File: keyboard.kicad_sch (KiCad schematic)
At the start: 207 parts, among them J2 USB_C_Receptacle_USB2.0_16P, J4 Conn_01x05, SW1 SW_Push, SW2 SW_Push, U1 RP2040, U2 XC6206PxxxMR, U3 W25Q128JVS, Y1 Crystal_GND24

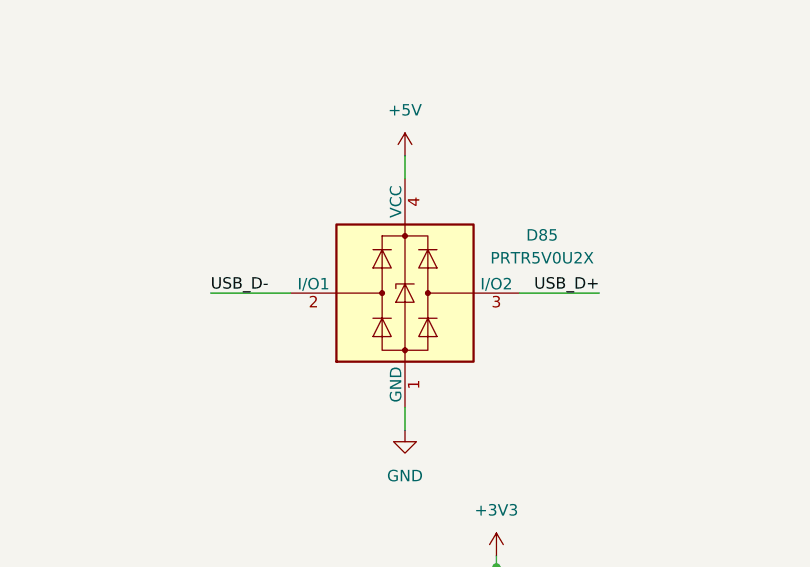
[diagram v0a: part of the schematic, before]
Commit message: add traces to usb subcircuit and subtraces
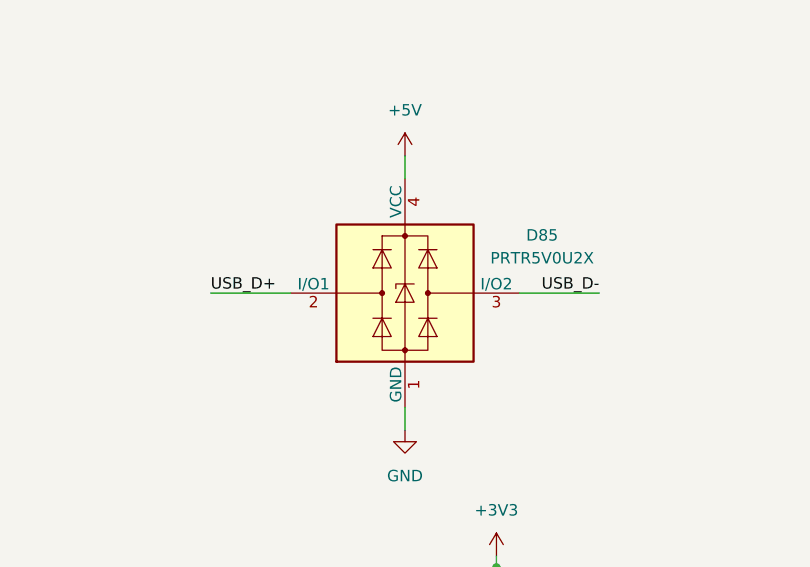
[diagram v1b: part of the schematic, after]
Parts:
- R1, R10, R11, R2, R6, R8, R9: footprint Resistor_SMD:R_0402_1005Metric -> Resistor_SMD:R_0402_1005Metric_Pad0.72x0.64mm_HandSolder
- R3, R7: footprint Resistor_SMD:R_0402_1005Metric -> Resistor_SMD:R_0805_2012Metric_Pad1.20x1.40mm_HandSolder
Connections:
- net USB_D+: now also D85.2 (I/O1); no longer D85.3 (I/O2)
- net USB_D-: now also D85.3 (I/O2); no longer D85.2 (I/O1)
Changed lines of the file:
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@@
 	)
 	(label "USB_D+"
-		(at 149.86 248.92 180)
+		(at 106.68 248.92 0)
 		(effects
 			(font
 				(size 1.27 1.27)
 			)
-			(justify right bottom)
+			(justify left bottom)
 		)
 	)
@@
 	)
 	(label "USB_D-"
-		(at 106.68 248.92 0)
+		(at 149.86 248.92 180)
 		(effects
 			(font
 				(size 1.27 1.27)
 			)
-			(justify left bottom)
+			(justify right bottom)
 		)
 	)
@@
 			)
 		)
-		(property "Footprint" "Resistor_SMD:R_0402_1005Metric"
+		(property "Footprint" "Resistor_SMD:R_0805_2012Metric_Pad1.20x1.40mm_HandSolder"
 			(at 88.9 187.96 0)
 			(hide yes)
@@
 			)
 		)
-		(property "Footprint" "Resistor_SMD:R_0402_1005Metric"
+		(property "Footprint" "Resistor_SMD:R_0402_1005Metric_Pad0.72x0.64mm_HandSolder"
 			(at 212.09 63.5 0)
 			(hide yes)
@@
 			)
 		)
-		(property "Footprint" "Resistor_SMD:R_0402_1005Metric"
+		(property "Footprint" "Resistor_SMD:R_0402_1005Metric_Pad0.72x0.64mm_HandSolder"
 			(at 299.72 60.96 0)
 			(hide yes)
@@
 			)
 		)
-		(property "Footprint" "Resistor_SMD:R_0402_1005Metric"
+		(property "Footprint" "Resistor_SMD:R_0402_1005Metric_Pad0.72x0.64mm_HandSolder"
 			(at 299.72 53.34 0)
 			(hide yes)
@@
 			)
 		)
-		(property "Footprint" "Resistor_SMD:R_0402_1005Metric"
+		(property "Footprint" "Resistor_SMD:R_0402_1005Metric_Pad0.72x0.64mm_HandSolder"
 			(at 82.55 91.948 90)
 			(hide yes)
@@
 			)
 		)
-		(property "Footprint" "Resistor_SMD:R_0402_1005Metric"
+		(property "Footprint" "Resistor_SMD:R_0402_1005Metric_Pad0.72x0.64mm_HandSolder"
 			(at 294.64 67.31 0)
 			(hide yes)
@@
 			)
 		)
-		(property "Footprint" "Resistor_SMD:R_0402_1005Metric"
+		(property "Footprint" "Resistor_SMD:R_0402_1005Metric_Pad0.72x0.64mm_HandSolder"
 			(at 82.55 83.058 90)
 			(hide yes)
@@
 			)
 		)
-		(property "Footprint" "Resistor_SMD:R_0402_1005Metric"
+		(property "Footprint" "Resistor_SMD:R_0402_1005Metric_Pad0.72x0.64mm_HandSolder"
 			(at 87.63 318.008 90)
 			(hide yes)
@@
 			)
 		)
-		(property "Footprint" "Resistor_SMD:R_0402_1005Metric"
+		(property "Footprint" "Resistor_SMD:R_0805_2012Metric_Pad1.20x1.40mm_HandSolder"
 			(at 96.52 185.42 0)
 			(hide yes)

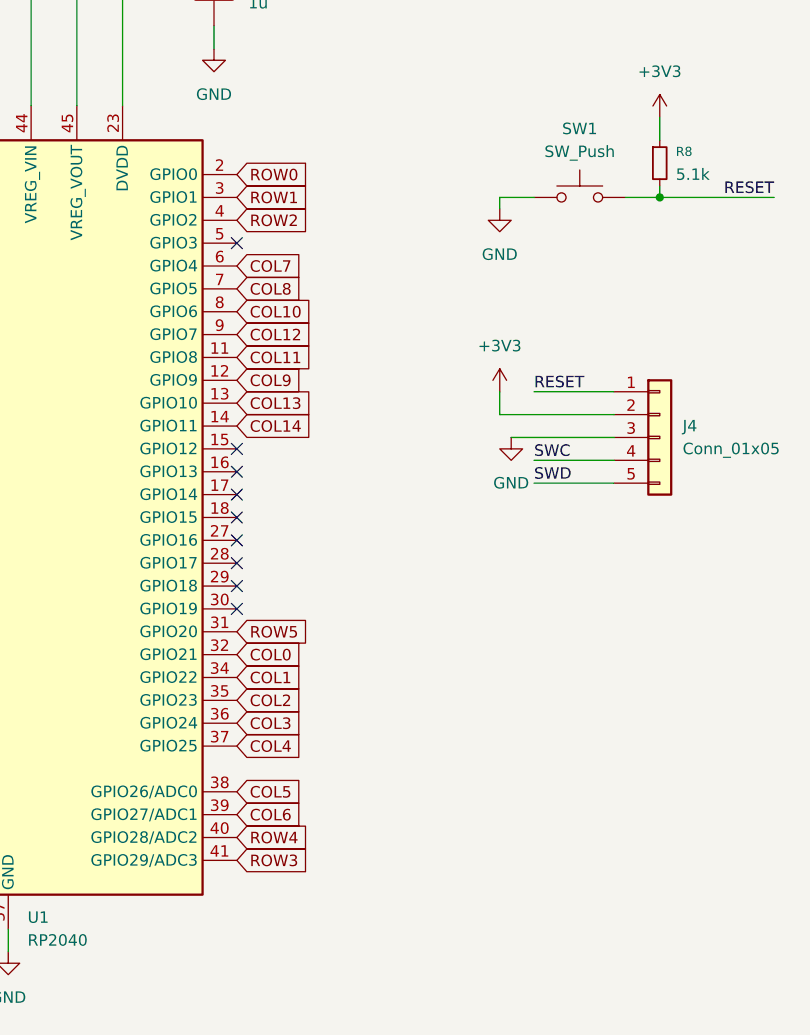
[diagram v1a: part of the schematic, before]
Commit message: routing complete, need to run DRC
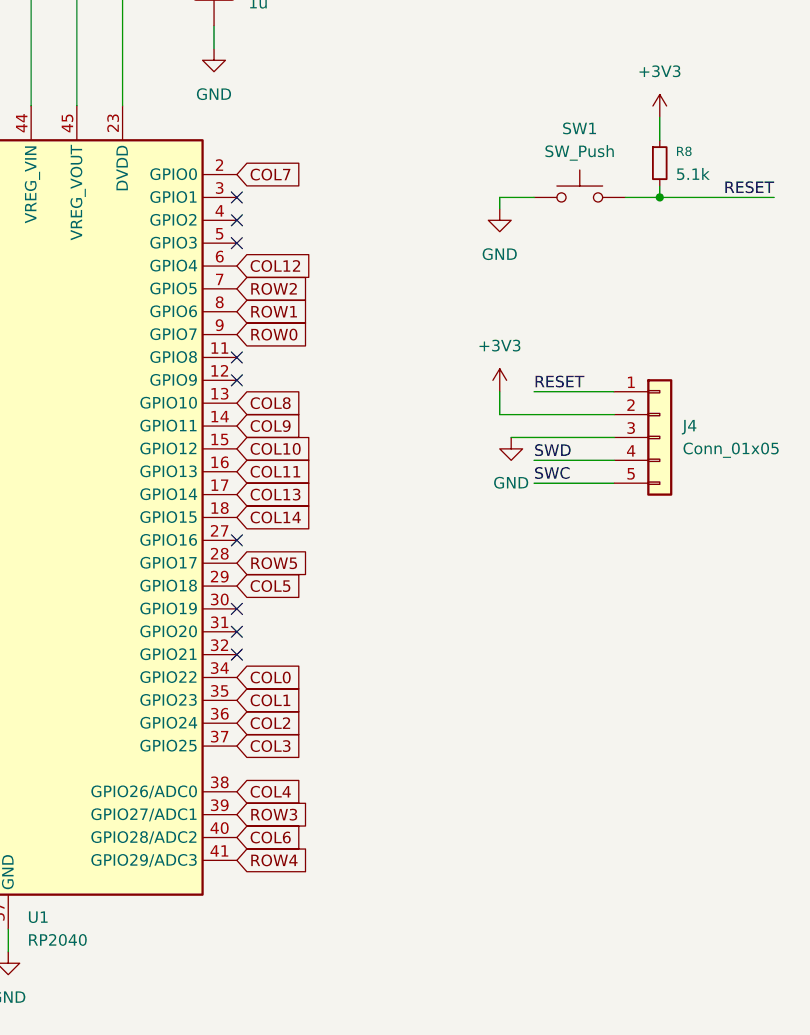
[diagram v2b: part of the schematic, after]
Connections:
- net COL0: now also U1.34 (GPIO22); no longer U1.32 (GPIO21)
- net COL1: now also U1.35 (GPIO23); no longer U1.34 (GPIO22)
- net COL10: now also U1.15 (GPIO12); no longer U1.8 (GPIO6)
- net COL11: now also U1.16 (GPIO13); no longer U1.11 (GPIO8)
- net COL12: now also U1.6 (GPIO4); no longer U1.9 (GPIO7)
- net COL13: now also U1.17 (GPIO14); no longer U1.13 (GPIO10)
- net COL14: now also U1.18 (GPIO15); no longer U1.14 (GPIO11)
- net COL2: now also U1.36 (GPIO24); no longer U1.35 (GPIO23)
- net COL3: now also U1.37 (GPIO25); no longer U1.36 (GPIO24)
- net COL4: now also U1.38 (GPIO26/ADC0); no longer U1.37 (GPIO25)
- net COL5: now also U1.29 (GPIO18); no longer U1.38 (GPIO26/ADC0)
- net COL6: now also U1.40 (GPIO28/ADC2); no longer U1.39 (GPIO27/ADC1)
- net COL7: now also U1.2 (GPIO0); no longer U1.6 (GPIO4)
- net COL8: now also U1.13 (GPIO10); no longer U1.7 (GPIO5)
- net COL9: now also U1.14 (GPIO11); no longer U1.12 (GPIO9)
- net ROW0: now also U1.9 (GPIO7); no longer U1.2 (GPIO0)
- net ROW1: now also U1.8 (GPIO6); no longer U1.3 (GPIO1)
- net ROW2: now also U1.7 (GPIO5); no longer U1.4 (GPIO2)
- net ROW3: now also U1.39 (GPIO27/ADC1); no longer U1.41 (GPIO29/ADC3)
- net ROW4: now also U1.41 (GPIO29/ADC3); no longer U1.40 (GPIO28/ADC2)
- net ROW5: now also U1.28 (GPIO17); no longer U1.31 (GPIO20)
- net SWC: now also J4.5 (Pin_5); no longer J4.4 (Pin_4)
- net SWD: now also J4.4 (Pin_4); no longer J4.5 (Pin_5)
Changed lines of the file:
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@@
 	)
 	(junction
-		(at 321.31 165.1)
-		(diameter 0)
-		(color 0 0 0 0)
-	)
-	(junction
 		(at 46.99 213.36)
 		(diameter 0)
@@
 	)
 	(junction
+		(at 321.31 165.1)
+		(diameter 0)
+		(color 0 0 0 0)
+	)
+	(junction
 		(at 304.8 184.15)
 		(diameter 0)
@@
 	)
 	(junction
-		(at 304.8 165.1)
-		(diameter 0)
-		(color 0 0 0 0)
-	)
-	(junction
 		(at 354.33 165.1)
 		(diameter 0)
@@
 	)
 	(junction
+		(at 304.8 165.1)
+		(diameter 0)
+		(color 0 0 0 0)
+	)
+	(junction
 		(at 105.41 173.99)
 		(diameter 0)
@@
 	)
 	(no_connect
-		(at 165.1 100.33)
+		(at 165.1 67.31)
 	)
 	(no_connect
-		(at 165.1 95.25)
+		(at 165.1 69.85)
 	)
 	(no_connect
-		(at 165.1 107.95)
+		(at 165.1 118.11)
 	)
 	(no_connect
-		(at 165.1 102.87)
+		(at 165.1 85.09)
 	)
 	(no_connect
-		(at 165.1 110.49)
+		(at 165.1 115.57)
 	)
 	(no_connect
-		(at 165.1 97.79)
+		(at 165.1 87.63)
 	)
 	(no_connect
@@
 	(wire
 		(pts
+			(xy 304.8 165.1) (xy 321.31 165.1)
+		)
+		(stroke
+			(width 0)
+			(type default)
+		)
+	)
+	(wire
+		(pts
 			(xy 469.9 203.2) (xy 518.16 203.2)
 		)
@@
 	(wire
 		(pts
-			(xy 304.8 165.1) (xy 321.31 165.1)
-		)
-		(stroke
-			(width 0)
-			(type default)
-		)
-	)
-	(wire
-		(pts
 			(xy 415.29 123.19) (xy 415.29 134.62)
 		)
@@
 	)
 	(label "SWD"
-		(at 198.12 99.06 0)
+		(at 198.12 96.52 0)
 		(effects
 			(font
@@
 	)
 	(label "SWC"
-		(at 198.12 96.52 0)
+		(at 198.12 99.06 0)
 		(effects
 			(font
@@
 	(global_label "COL2"
 		(shape input)
-		(at 165.1 123.19 0)
+		(at 165.1 125.73 0)
 		(fields_autoplaced yes)
 		(effects
@@
 		)
 		(property "Intersheetrefs" "${INTERSHEET_REFS}"
-			(at 172.9233 123.19 0)
+			(at 172.9233 125.73 0)
 			(hide yes)
 			(show_name no)
@@
 	(global_label "ROW5"
 		(shape input)
-		(at 165.1 115.57 0)
+		(at 165.1 107.95 0)
 		(fields_autoplaced yes)
 		(effects
@@
 		)
 		(property "Intersheetrefs" "${INTERSHEET_REFS}"
-			(at 172.9233 115.57 0)
+			(at 172.9233 107.95 0)
 			(hide yes)
 			(show_name no)
@@
 	(global_label "COL0"
 		(shape input)
-		(at 165.1 118.11 0)
+		(at 165.1 120.65 0)
 		(fields_autoplaced yes)
 		(effects
@@
 		)
 		(property "Intersheetrefs" "${INTERSHEET_REFS}"
-			(at 173.3466 118.11 0)
+			(at 173.3466 120.65 0)
 			(hide yes)
 			(show_name no)
@@
 	(global_label "COL12"
 		(shape input)
-		(at 165.1 82.55 0)
+		(at 165.1 74.93 0)
 		(fields_autoplaced yes)
 		(effects
@@
 		)
 		(property "Intersheetrefs" "${INTERSHEET_REFS}"
-			(at 172.9233 82.55 0)
+			(at 174.1328 74.93 0)
 			(hide yes)
 			(show_name no)
@@
 	(global_label "ROW1"
 		(shape input)
-		(at 165.1 67.31 0)
+		(at 165.1 80.01 0)
 		(fields_autoplaced yes)
 		(effects
@@
 		)
 		(property "Intersheetrefs" "${INTERSHEET_REFS}"
-			(at 173.3466 67.31 0)
+			(at 173.3466 80.01 0)
 			(hide yes)
 			(show_name no)
@@
 	(global_label "COL4"
 		(shape input)
-		(at 165.1 128.27 0)
+		(at 165.1 133.35 0)
 		(fields_autoplaced yes)
 		(effects
@@
 		)
 		(property "Intersheetrefs" "${INTERSHEET_REFS}"
-			(at 172.9233 128.27 0)
+			(at 172.9233 133.35 0)
 			(hide yes)
 			(show_name no)
@@
 	(global_label "ROW3"
 		(shape input)
-		(at 165.1 140.97 0)
+		(at 165.1 135.89 0)
 		(fields_autoplaced yes)
 		(effects
@@
 		)
 		(property "Intersheetrefs" "${INTERSHEET_REFS}"
-			(at 173.3466 140.97 0)
+			(at 172.9233 135.89 0)
 			(hide yes)
 			(show_name no)
@@
 	(global_label "COL11"
 		(shape input)
-		(at 165.1 85.09 0)
+		(at 165.1 97.79 0)
 		(fields_autoplaced yes)
 		(effects
@@
 		)
 		(property "Intersheetrefs" "${INTERSHEET_REFS}"
-			(at 172.9233 85.09 0)
+			(at 172.9233 97.79 0)
 			(hide yes)
 			(show_name no)
@@
 	(global_label "COL10"
 		(shape input)
-		(at 165.1 80.01 0)
+		(at 165.1 95.25 0)
 		(fields_autoplaced yes)
 		(effects
@@
 		)
 		(property "Intersheetrefs" "${INTERSHEET_REFS}"
-			(at 174.1328 80.01 0)
+			(at 172.9233 95.25 0)
 			(hide yes)
 			(show_name no)
@@
 	(global_label "ROW0"
 		(shape input)
-		(at 165.1 64.77 0)
+		(at 165.1 82.55 0)
 		(fields_autoplaced yes)
 		(effects
@@
 		)
 		(property "Intersheetrefs" "${INTERSHEET_REFS}"
-			(at 173.3466 64.77 0)
+			(at 174.1328 82.55 0)
 			(hide yes)
 			(show_name no)
@@
 	(global_label "COL5"
 		(shape input)
-		(at 165.1 133.35 0)
+		(at 165.1 110.49 0)
 		(fields_autoplaced yes)
 		(effects
@@
 		)
 		(property "Intersheetrefs" "${INTERSHEET_REFS}"
-			(at 172.9233 133.35 0)
+			(at 173.3466 110.49 0)
 			(hide yes)
 			(show_name no)
@@
 	(global_label "ROW4"
 		(shape input)
-		(at 165.1 138.43 0)
+		(at 165.1 140.97 0)
 		(fields_autoplaced yes)
 		(effects
@@
 		)
 		(property "Intersheetrefs" "${INTERSHEET_REFS}"
-			(at 172.9233 138.43 0)
+			(at 173.3466 140.97 0)
 			(hide yes)
 			(show_name no)
@@
 	(global_label "COL3"
 		(shape input)
-		(at 165.1 125.73 0)
+		(at 165.1 128.27 0)
 		(fields_autoplaced yes)
 		(effects
@@
 		)
 		(property "Intersheetrefs" "${INTERSHEET_REFS}"
-			(at 172.9233 125.73 0)
+			(at 172.9233 128.27 0)
 			(hide yes)
 			(show_name no)
@@
 	(global_label "COL14"
 		(shape input)
-		(at 165.1 92.71 0)
+		(at 165.1 102.87 0)
 		(fields_autoplaced yes)
 		(effects
@@
 		)
 		(property "Intersheetrefs" "${INTERSHEET_REFS}"
-			(at 174.1328 92.71 0)
+			(at 174.1328 102.87 0)
 			(hide yes)
 			(show_name no)
@@
 	(global_label "COL7"
 		(shape input)
-		(at 165.1 74.93 0)
+		(at 165.1 64.77 0)
 		(fields_autoplaced yes)
 		(effects
@@
 		)
 		(property "Intersheetrefs" "${INTERSHEET_REFS}"
-			(at 174.1328 74.93 0)
+			(at 173.3466 64.77 0)
 			(hide yes)
 			(show_name no)
@@
 	(global_label "ROW2"
 		(shape input)
-		(at 165.1 69.85 0)
+		(at 165.1 77.47 0)
 		(fields_autoplaced yes)
 		(effects
@@
 		)
 		(property "Intersheetrefs" "${INTERSHEET_REFS}"
-			(at 173.3466 69.85 0)
+			(at 173.3466 77.47 0)
 			(hide yes)
 			(show_name no)
@@
 	(global_label "COL8"
 		(shape input)
-		(at 165.1 77.47 0)
+		(at 165.1 90.17 0)
 		(fields_autoplaced yes)
 		(effects
@@
 		)
 		(property "Intersheetrefs" "${INTERSHEET_REFS}"
-			(at 174.1328 77.47 0)
+			(at 172.9233 90.17 0)
 			(hide yes)
 			(show_name no)
@@
 	(global_label "COL1"
 		(shape input)
-		(at 165.1 120.65 0)
+		(at 165.1 123.19 0)
 		(fields_autoplaced yes)
 		(effects
@@
 		)
 		(property "Intersheetrefs" "${INTERSHEET_REFS}"
-			(at 173.3466 120.65 0)
+			(at 172.9233 123.19 0)
 			(hide yes)
 			(show_name no)
@@
 	(global_label "COL6"
 		(shape input)
-		(at 165.1 135.89 0)
+		(at 165.1 138.43 0)
 		(fields_autoplaced yes)
 		(effects
@@
 		)
 		(property "Intersheetrefs" "${INTERSHEET_REFS}"
-			(at 172.9233 135.89 0)
+			(at 172.9233 138.43 0)
 			(hide yes)
 			(show_name no)
@@
 	(global_label "COL13"
 		(shape input)
-		(at 165.1 90.17 0)
+		(at 165.1 100.33 0)
 		(fields_autoplaced yes)
 		(effects
@@
 		)
 		(property "Intersheetrefs" "${INTERSHEET_REFS}"
-			(at 174.1328 90.17 0)
+			(at 174.1328 100.33 0)
 			(hide yes)
 			(show_name no)
@@
 	(global_label "COL9"
 		(shape input)
-		(at 165.1 87.63 0)
+		(at 165.1 92.71 0)
 		(fields_autoplaced yes)
 		(effects
@@
 		)
 		(property "Intersheetrefs" "${INTERSHEET_REFS}"
-			(at 172.9233 87.63 0)
+			(at 174.1328 92.71 0)
 			(hide yes)
 			(show_name no)

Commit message: clean up schematic
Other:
- note added: "Crystal Oscillator"
- note added: "Debug Header"
- note added: "ESD Protection"
- note added: "Flash Chip"
- note added: "Keyboard Matrix"
- note added: "RP2040"
- note added: "USB-C Port"
- moved on the sheet: C1, C10, C11, C12, C13, C14, C15, C16, C2, C3, C4, C5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

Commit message: swap to hotswappable sockets, may not adjust components
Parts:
- MX1, MX10, MX11, MX12, MX13, MX14, MX15, MX16, MX17, MX18, MX19, MX2, MX20, MX21, MX22, MX23, MX24, MX25, MX26, MX27, MX28, MX29, MX3, MX30, MX31, MX33, MX34, MX35, MX36, MX37, MX38, MX39, MX4, MX40, MX41, MX42, MX43, MX44, MX46, MX48, MX49, MX5, MX50, MX51, MX52, MX53, MX54, MX55, MX56, MX57, MX58, MX59, MX6, MX60, MX61, MX62, MX63, MX64, MX65, MX66, MX67, MX68, MX69, MX7, MX70, MX71, MX73, MX74, MX78, MX79, MX8, MX80, MX81, MX82, MX83, MX84, MX9: footprint PCM_marbastlib-mx:SW_MX_1u -> PCM_marbastlib-mx:SW_MX_HS_CPG151101S11_1u
- MX32, MX45: footprint PCM_marbastlib-mx:SW_MX_1.5u -> PCM_marbastlib-mx:SW_MX_HS_CPG151101S11_1.5u
- MX47, MX72: footprint PCM_marbastlib-mx:SW_MX_1.75u -> PCM_marbastlib-mx:SW_MX_HS_CPG151101S11_1.75u
- MX75, MX76, MX77: footprint PCM_marbastlib-mx:SW_MX_1.25u -> PCM_marbastlib-mx:SW_MX_HS_CPG151101S11_1.25u

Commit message: add separate LED daisy link sch
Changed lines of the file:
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@@
 	(wire
 		(pts
-			(xy 33.02 393.7) (xy 33.02 394.97)
+			(xy 91.44 287.02) (xy 91.44 288.29)
 		)
 		(stroke
@@
 	(wire
 		(pts
-			(xy 46.99 393.7) (xy 46.99 394.97)
+			(xy 105.41 287.02) (xy 105.41 288.29)
 		)
 		(stroke
@@
 	(wire
 		(pts
-			(xy 59.69 393.7) (xy 59.69 394.97)
+			(xy 118.11 287.02) (xy 118.11 288.29)
 		)
 		(stroke
@@
 	(symbol
 		(lib_id "power:PWR_FLAG")
-		(at 59.69 393.7 0)
+		(at 118.11 287.02 0)
 		(unit 1)
 		(body_style 1)
@@
 		(fields_autoplaced yes)
 		(property "Reference" "#FLG03"
-			(at 59.69 391.795 0)
+			(at 118.11 285.115 0)
 			(hide yes)
 			(show_name no)
@@
 		)
 		(property "Value" "PWR_FLAG"
-			(at 59.69 388.62 0)
+			(at 118.11 281.94 0)
 			(show_name no)
 			(do_not_autoplace no)
@@
 		)
 		(property "Footprint" ""
-			(at 59.69 393.7 0)
+			(at 118.11 287.02 0)
 			(hide yes)
 			(show_name no)
@@
 		)
 		(property "Datasheet" ""
-			(at 59.69 393.7 0)
+			(at 118.11 287.02 0)
 			(hide yes)
 			(show_name no)
@@
 		)
 		(property "Description" "Special symbol for telling ERC where power comes from"
-			(at 59.69 393.7 0)
+			(at 118.11 287.02 0)
 			(hide yes)
 			(show_name no)
@@
 	(symbol
 		(lib_id "power:PWR_FLAG")
-		(at 33.02 393.7 0)
+		(at 91.44 287.02 0)
 		(unit 1)
 		(body_style 1)
@@
 		(fields_autoplaced yes)
 		(property "Reference" "#FLG01"
-			(at 33.02 391.795 0)
+			(at 91.44 285.115 0)
 			(hide yes)
 			(show_name no)
@@
 		)
 		(property "Value" "PWR_FLAG"
-			(at 33.02 388.62 0)
+			(at 91.44 281.94 0)
 			(show_name no)
 			(do_not_autoplace no)
@@
 		)
 		(property "Footprint" ""
-			(at 33.02 393.7 0)
+			(at 91.44 287.02 0)
 			(hide yes)
 			(show_name no)
@@
 		)
 		(property "Datasheet" ""
-			(at 33.02 393.7 0)
+			(at 91.44 287.02 0)
 			(hide yes)
 			(show_name no)
@@
 		)
 		(property "Description" "Special symbol for telling ERC where power comes from"
-			(at 33.02 393.7 0)
+			(at 91.44 287.02 0)
 			(hide yes)
 			(show_name no)
@@
 	(symbol
 		(lib_id "power:PWR_FLAG")
-		(at 46.99 393.7 0)
+		(at 105.41 287.02 0)
 		(unit 1)
 		(body_style 1)
@@
 		(fields_autoplaced yes)
 		(property "Reference" "#FLG02"
-			(at 46.99 391.795 0)
+			(at 105.41 285.115 0)
 			(hide yes)
 			(show_name no)
@@
 		)
 		(property "Value" "PWR_FLAG"
-			(at 46.99 388.62 0)
+			(at 105.41 281.94 0)
 			(show_name no)
 			(do_not_autoplace no)
@@
 		)
 		(property "Footprint" ""
-			(at 46.99 393.7 0)
+			(at 105.41 287.02 0)
 			(hide yes)
 			(show_name no)
@@
 		)
 		(property "Datasheet" ""
-			(at 46.99 393.7 0)
+			(at 105.41 287.02 0)
 			(hide yes)
 			(show_name no)
@@
 		)
 		(property "Description" "Special symbol for telling ERC where power comes from"
-			(at 46.99 393.7 0)
+			(at 105.41 287.02 0)
 			(hide yes)
 			(show_name no)
@@
 	(symbol
 		(lib_id "power:VBUS")
-		(at 46.99 394.97 180)
+		(at 105.41 288.29 180)
 		(unit 1)
 		(body_style 1)
@@
 		(fields_autoplaced yes)
 		(property "Reference" "#PWR033"
-			(at 46.99 391.16 0)
+			(at 105.41 284.48 0)
 			(hide yes)
 			(show_name no)
@@
 		)
 		(property "Value" "VBUS"
-			(at 46.99 400.05 0)
+			(at 105.41 293.37 0)
 			(show_name no)
 			(do_not_autoplace no)
@@
 		)
 		(property "Footprint" ""
-			(at 46.99 394.97 0)
+			(at 105.41 288.29 0)
 			(hide yes)
 			(show_name no)
@@
 		)
 		(property "Datasheet" ""
-			(at 46.99 394.97 0)
+			(at 105.41 288.29 0)
 			(hide yes)
 			(show_name no)
@@
 		)
 		(property "Description" "Power symbol creates a global label with name \"VBUS\""
-			(at 46.99 394.97 0)
+			(at 105.41 288.29 0)
 			(hide yes)
 			(show_name no)
@@
 	(symbol
 		(lib_id "power:+5V")
-		(at 59.69 394.97 180)
+		(at 118.11 288.29 180)
 		(unit 1)
 		(body_style 1)
@@
 		(fields_autoplaced yes)
 		(property "Reference" "#PWR034"
-			(at 59.69 391.16 0)
+			(at 118.11 284.48 0)
 			(hide yes)
 			(show_name no)
@@
 		)
 		(property "Value" "+5V"
-			(at 59.69 400.05 0)
+			(at 118.11 293.37 0)
 			(show_name no)
 			(do_not_autoplace no)
@@
 		)
 		(property "Footprint" ""
-			(at 59.69 394.97 0)
+			(at 118.11 288.29 0)
 			(hide yes)
 			(show_name no)
@@
 		)
 		(property "Datasheet" ""
-			(at 59.69 394.97 0)
+			(at 118.11 288.29 0)
 			(hide yes)
 			(show_name no)
@@
 		)
 		(property "Description" "Power symbol creates a global label with name \"+5V\""
-			(at 59.69 394.97 0)
+			(at 118.11 288.29 0)
 			(hide yes)
 			(show_name no)
@@
 	(symbol
 		(lib_id "power:GND")
-		(at 33.02 394.97 0)
+		(at 91.44 288.29 0)
 		(unit 1)
 		(body_style 1)
@@
 		(fields_autoplaced yes)
 		(property "Reference" "#PWR019"
-			(at 33.02 401.32 0)
+			(at 91.44 294.64 0)
 			(hide yes)
 			(show_name no)
@@
 		)
 		(property "Value" "GND"
-			(at 33.02 400.05 0)
+			(at 91.44 293.37 0)
 			(show_name no)
 			(do_not_autoplace no)
@@
 		)
 		(property "Footprint" ""
-			(at 33.02 394.97 0)
+			(at 91.44 288.29 0)
 			(hide yes)
 			(show_name no)
@@
 		)
 		(property "Datasheet" ""
-			(at 33.02 394.97 0)
+			(at 91.44 288.29 0)
 			(hide yes)
 			(show_name no)
@@
 		)
 		(property "Description" "Power symbol creates a global label with name \"GND\" , ground"
-			(at 33.02 394.97 0)
+			(at 91.44 288.29 0)
 			(hide yes)
 			(show_name no)
